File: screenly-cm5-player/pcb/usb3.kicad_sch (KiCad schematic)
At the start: 20 parts, among them J8 HYCW275-USBC24-050B, U8 AP22652W6-7, U9 HD3SS3220IRNHR

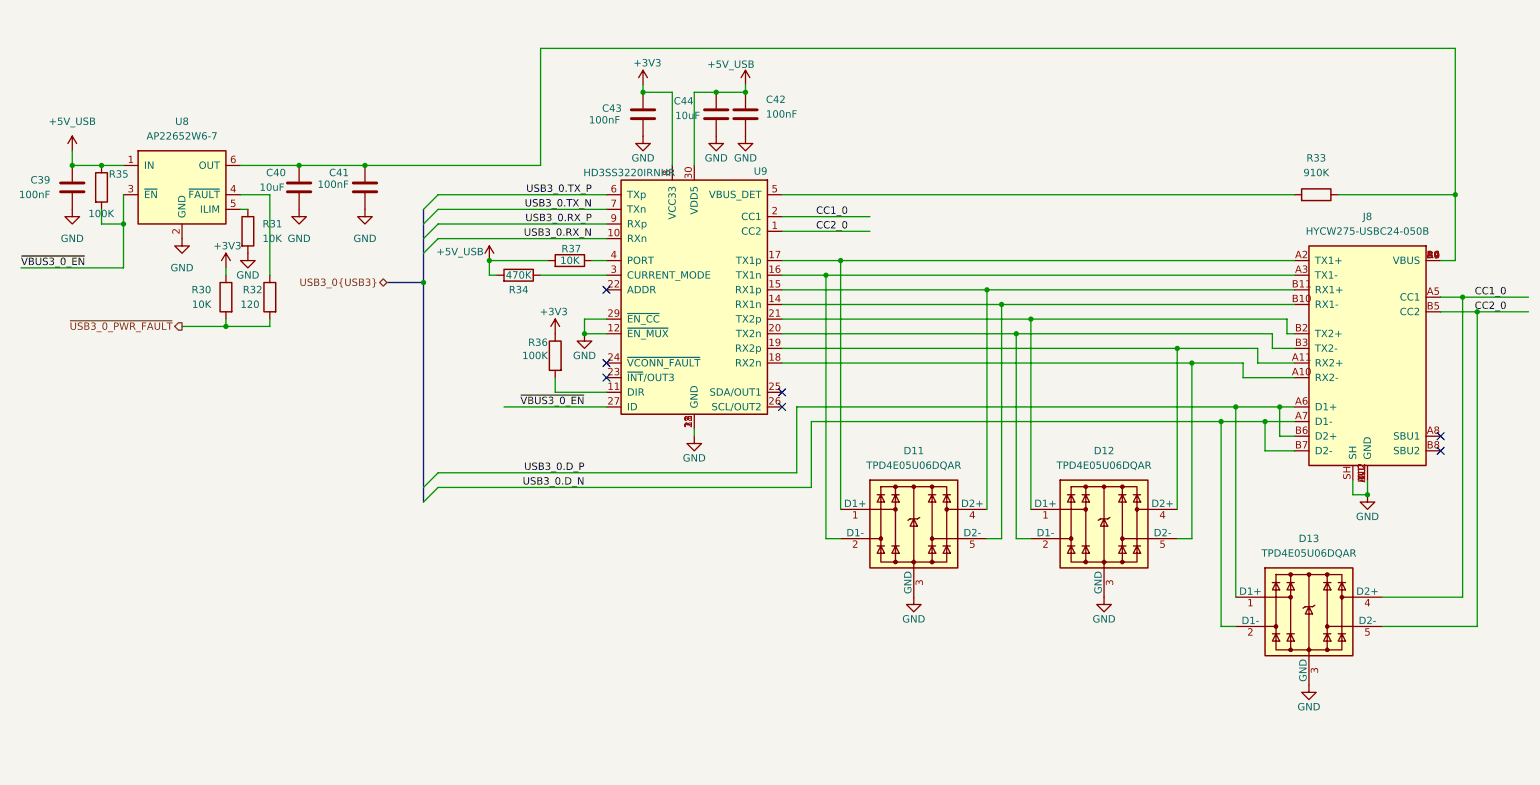
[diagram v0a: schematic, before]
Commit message: Revised USB design 1xUSB-C 2.0, 2xUSB-A 3.0
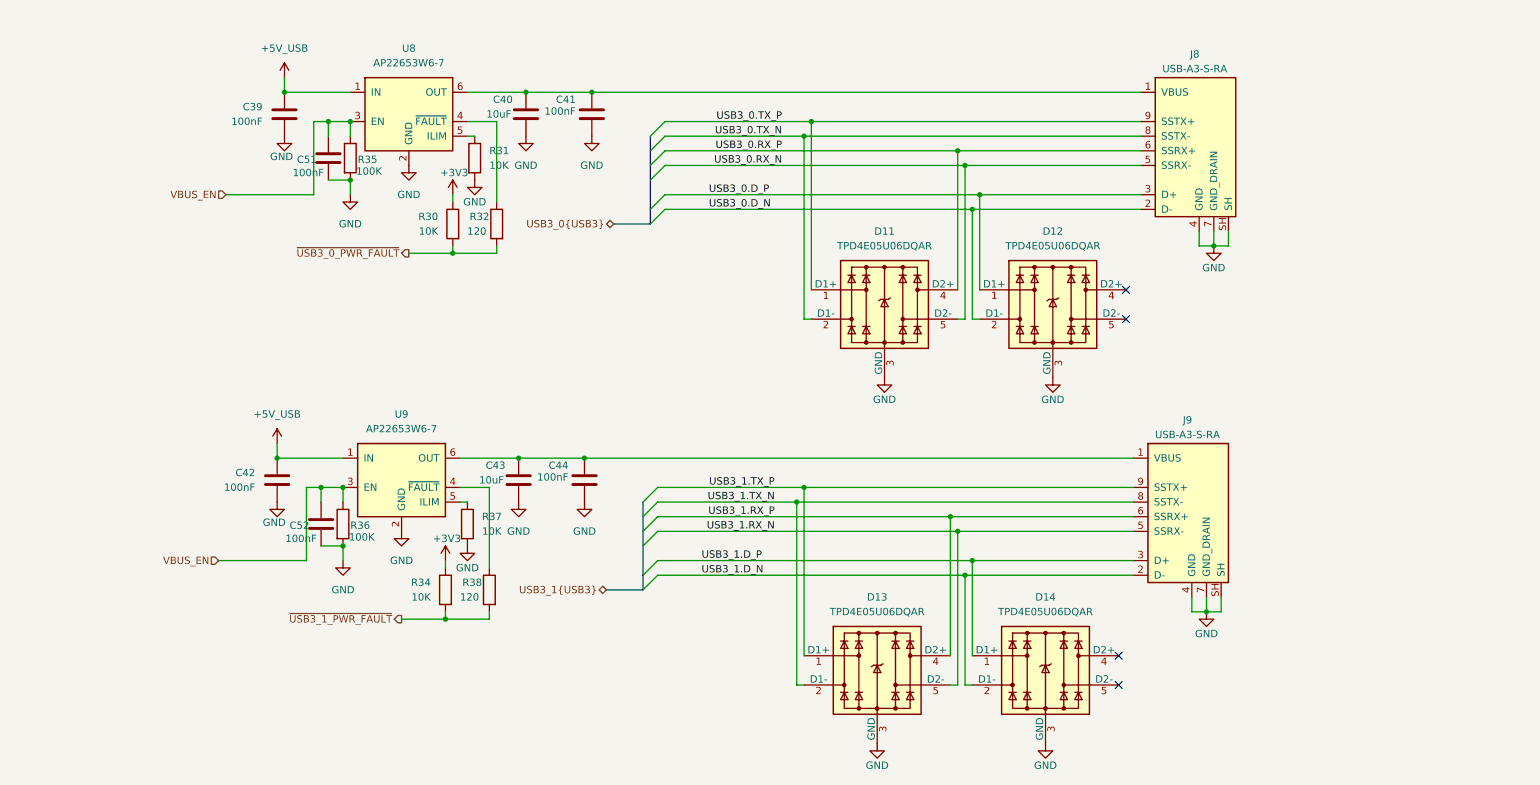
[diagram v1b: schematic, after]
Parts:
- removed C43: 100nF, Screenly:C_0402, symbol Screenly:Capacitor 100nF 50V X7R 0402 (CL05B104KB54PNC)
- removed C44: 10uF, Screenly:C_1210, symbol Screenly:Capacitor 10uF 50V X7R 1210 (CL32B106KBJNNNE)
- removed J8: HYCW275-USBC24-050B, Screenly:USB_C_Receptacle_HOAUC_HYCW275-USBC24-050B, symbol Screenly:USB-C Receptacle 24P USB 3.1 SMD (HYCW275-USBC24-050B)
- removed R33: 910K, Screenly:R_0402, symbol Screenly:Resistor 910K 1% 0402 (0402WGF9103TCE)
- removed R34: 470K, Screenly:R_0402, symbol Screenly:Resistor 470K 5% 0402 (0402WGJ0474TCE)
- removed U8: AP22652W6-7, Screenly:SOT-23-6, symbol Screenly:Power Switch 3-5.5V 2.1A SOT-23-6 (AP22652W6-7)
- removed U9: HD3SS3220IRNHR, Screenly:TI_WQFN-30-1EP_2.5x4.5mm_P0.4mm_EP1.2x3.2mm, symbol Screenly:USB SS Mux IC Type-C Port Controller 10Gbps WQFN-30 (HD3SS3220IRNHR)
- added C43: 10uF, Screenly:C_1210, symbol Screenly:Capacitor 10uF 50V X7R 1210 (CL32B106KBJNNNE)
- added C44, C51, C52: 100nF, Screenly:C_0402, symbol Screenly:Capacitor 100nF 50V X7R 0402 (CL05B104KB54PNC)
- added D14: TPD4E05U06DQAR, Screenly:TI_USON-10_2.5x1.0mm_P0.5mm, symbol Screenly:ESD Diode 4ch 5.5V USON-10 (TPD4E05U06DQAR)
- added J8, J9: USB-A3-S-RA, Screenly:USB_A_USB3_AdamTech_USB-A3-S-RA_Horizontal, symbol Screenly:USB-A Receptacle USB 3.0 THT (USB-A3-S-RA)
- added R34: 10K, Screenly:R_0402, symbol Screenly:Resistor 10K 1% 0402 (RC0402FR-0710KL)
- added R38: 120, Screenly:R_0402, symbol Screenly:Resistor 120R 5% 0402 (0402WGJ0121TCE)
- added U8, U9: AP22653W6-7, Screenly:SOT-23-6, symbol Screenly:Power Switch 3-5.5V 2.1A SOT-23-6 (AP22653W6-7)
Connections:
- net ~{VBUS3_0_EN} is gone; now on net GND: R35.2
- net +3V3: now also R34.1; no longer R36.1
- net +5V_USB: now also U8.1 (IN), U9.1 (IN); no longer R35.1, R37.2
- net GND: now also R36.2, R37.2, C43.2, C44.2, C51.2, C52.2, D14.3 (GND), D14.8 (GND), J8.4 (GND), J8.7 (GND_DRAIN), J8.SH, J9.4 (GND), J9.7 (GND_DRAIN), J9.SH, U8.2 (GND), U9.2 (GND)
- net USB3_0.D_N: now also D12.2 (D1-), D12.9, J8.2 (D-); no longer D13.2 (D1-), D13.9
- net USB3_0.D_P: now also D12.1 (D1+), D12.10, J8.3 (D+); no longer D13.1 (D1+), D13.10
- net USB3_0.RX_N: now also D11.5 (D2-), D11.6, J8.5 (SSRX-)
- net USB3_0.RX_P: now also D11.4 (D2+), D11.7, J8.6 (SSRX+)
- net USB3_0.TX_N: now also D11.2 (D1-), D11.9, J8.8 (SSTX-)
- net USB3_0.TX_P: now also D11.1 (D1+), D11.10, J8.9 (SSTX+)
- net at R32.1: now also U8.4 (~{FAULT})
- net at R31.1: now also U8.5 (ILIM)
- net at C40.1, C41.1: now also J8.1 (VBUS), U8.6 (OUT)
- net at R37.1: now also U9.5 (ILIM)
- net CC1_0 renamed USB3_1.RX_P
- net USB3_1.RX_P: now also J9.6 (SSRX+)
- net CC2_0 renamed USB3_1.RX_N
- net USB3_1.RX_N: now also J9.5 (SSRX-)
- new net: R38.1, U9.4 (~{FAULT})
- new net: C43.1, C44.1, J9.1 (VBUS), U9.6 (OUT)
- new net: D14.4 (D2+), D14.7
- new net: D14.5 (D2-), D14.6
- new net USB3_1.D_N: D14.2 (D1-), D14.9, J9.2 (D-)
- new net USB3_1.D_P: D14.1 (D1+), D14.10, J9.3 (D+)
- new net USB3_1.TX_N: D13.2 (D1-), D13.9, J9.8 (SSTX-)
- new net USB3_1.TX_P: D13.1 (D1+), D13.10, J9.9 (SSTX+)
- new net VBUS_EN: C51.1, C52.1, R35.1, R36.1, U8.3 (EN), U9.3 (EN)
- new net ~{USB3_1_PWR_FAULT}: R34.2, R38.2
- no-connect marks 7 -> 4
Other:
- moved on the sheet: C39, C40, C41, D11, D12, R30, R31, R32, R35

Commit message: Finished schematics design.
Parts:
- added TP15, TP16: TestPoint, Screenly:TestPoint_Pad_D2.0mm, symbol Screenly:Test Point Pad 2.0mm
- renumbered C39 to C35, C42 to C36, C51 to C37, C52 to C38, C40 to C39, C43 to C40, C44 to C42, D13 to D12, D12 to D13, R35 to R33, R36 to R34, R30 to R35, R34 to R36, R31 to R37, R37 to R38, R32 to R39, R38 to R40, U8 to U7, U9 to U8
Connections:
- net USB3_0.RX_N: no longer D11.6
- net USB3_0.RX_P: no longer D11.7
- net USB3_1.RX_N: no longer D12.6
- net USB3_1.RX_P: no longer D12.7
- net at C39.1, C41.1, J8.1 (VBUS)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: now also TP15.1
- net at C40.1, C42.1, J9.1 (VBUS)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: now also TP16.1
- net at D14.4 (D2+): no longer D14.7
- net at D14.5 (D2-): no longer D14.6
- net at D13.4 (D2+): no longer D13.7
- net at D13.5 (D2-): no longer D13.6
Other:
- moved on the sheet: C35, C37, C39, C41, D11, D13, J8, R33, R35, R37, R39, U7

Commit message: Rough placements
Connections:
- net USB3_0.RX_N: now also D11.6
- net USB3_0.RX_P: now also D11.7
- net USB3_1.RX_N: now also D12.6
- net USB3_1.RX_P: now also D12.7
- net at D14.4 (D2+): now also D14.7
- net at D14.5 (D2-): now also D14.6
- net at D13.4 (D2+): now also D13.7
- net at D13.5 (D2-): now also D13.6
